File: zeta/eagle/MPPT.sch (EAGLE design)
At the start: 52 parts, among them J1 1.27MM-SWD-CONNECTOR, Q1 ON-NFET, Q2 P-CHANNELFET, U1 TCAN330, U3 LM3671MF-3.3, U6 STM32F042K6, X1 8MHZ-2.5x2mm

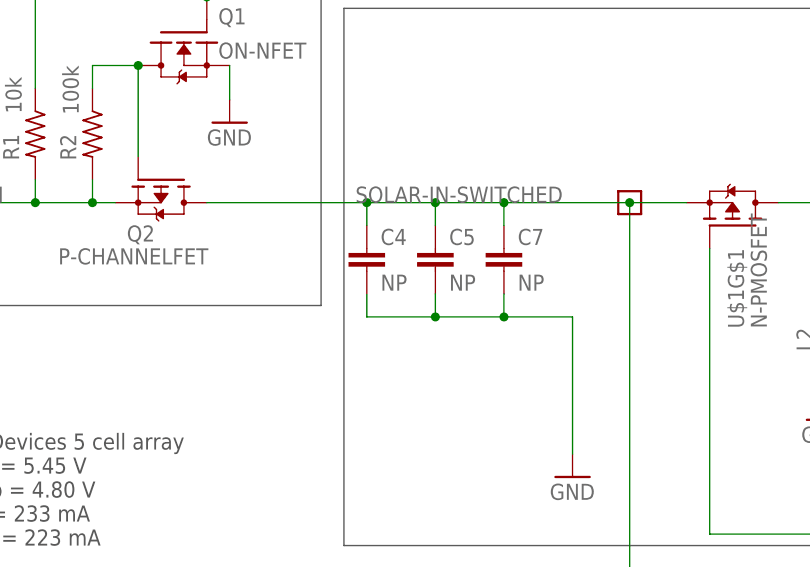
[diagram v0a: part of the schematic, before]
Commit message: Added Breakout Cable Schematic
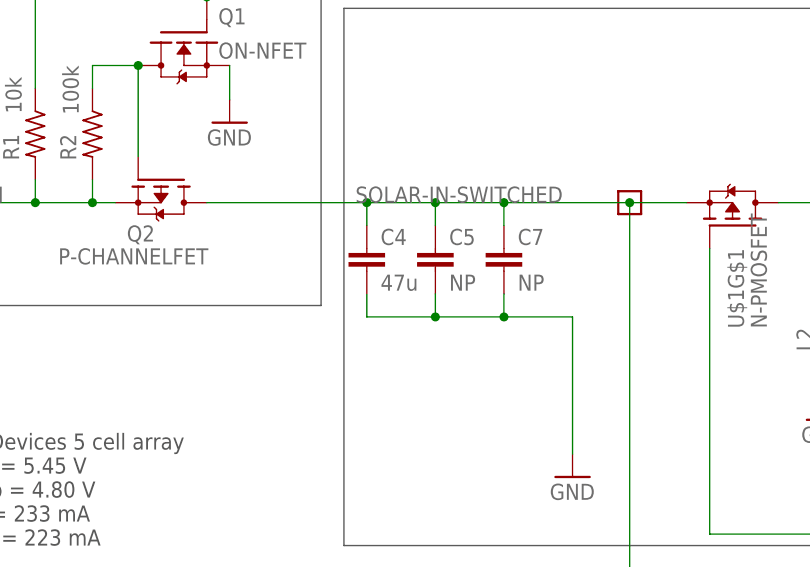
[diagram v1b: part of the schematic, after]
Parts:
- C4: value NP -> 47u
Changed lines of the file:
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@@
 <setting verticaltext="up"/>
 </settings>
-<grid distance="1.27" unitdist="mm" unit="mm" style="lines" multiple="1" display="no" altdistance="0.01" altunitdist="inch" altunit="inch"/>
+<grid distance="0.1" unitdist="inch" unit="inch" style="lines" multiple="1" display="no" altdistance="0.01" altunitdist="inch" altunit="inch"/>
 <layers>
-<layer number="1" name="Top" color="4" fill="1" visible="yes" active="no"/>
-<layer number="2" name="Route2" color="15" fill="1" visible="yes" active="no"/>
-<layer number="3" name="Route3" color="4" fill="3" visible="yes" active="no"/>
-<layer number="4" name="Route4" color="1" fill="4" visible="yes" active="no"/>
-<layer number="5" name="Route5" color="4" fill="4" visible="yes" active="no"/>
-<layer number="6" name="Route6" color="1" fill="8" visible="yes" active="no"/>
-<layer number="7" name="Route7" color="4" fill="8" visible="yes" active="no"/>
-<layer number="8" name="Route8" color="1" fill="2" visible="yes" active="no"/>
-<layer number="9" name="Route9" color="4" fill="2" visible="yes" active="no"/>
-<layer number="10" name="Route10" color="1" fill="7" visible="yes" active="no"/>
-<layer number="11" name="Route11" color="4" fill="7" visible="yes" active="no"/>
-<layer number="12" name="Route12" color="1" fill="5" visible="yes" active="no"/>
-<layer number="13" name="Route13" color="4" fill="5" visible="yes" active="no"/>
-<layer number="14" name="Route14" color="1" fill="6" visible="yes" active="no"/>
-<layer number="15" name="Route15" color="14" fill="1" visible="yes" active="no"/>
-<layer number="16" name="Bottom" color="1" fill="1" visible="yes" active="no"/>
-<layer number="17" name="Pads" color="2" fill="1" visible="yes" active="no"/>
-<layer number="18" name="Vias" color="2" fill="1" visible="yes" active="no"/>
-<layer number="19" name="Unrouted" color="6" fill="1" visible="yes" active="no"/>
-<layer number="20" name="Dimension" color="15" fill="1" visible="yes" active="no"/>
-<layer number="21" name="tPlace" color="7" fill="1" visible="yes" active="no"/>
-<layer number="22" name="bPlace" color="7" fill="1" visible="yes" active="no"/>
-<layer number="23" name="tOrigins" color="15" fill="1" visible="yes" active="no"/>
-<layer number="24" name="bOrigins" color="15" fill="1" visible="yes" active="no"/>
-<layer number="25" name="tNames" color="7" fill="1" visible="yes" active="no"/>
-<layer number="26" name="bNames" color="7" fill="1" visible="yes" active="no"/>
-<layer number="27" name="tValues" color="7" fill="1" visible="yes" active="no"/>
-<layer number="28" name="bValues" color="7" fill="1" visible="yes" active="no"/>
+<layer number="1" name="Top" color="4" fill="1" visible="no" active="no"/>
+<layer number="2" name="Route2" color="15" fill="1" visible="no" active="no"/>
+<layer number="3" name="Route3" color="4" fill="3" visible="no" active="no"/>
+<layer number="4" name="Route4" color="1" fill="4" visible="no" active="no"/>
+<layer number="5" name="Route5" color="4" fill="4" visible="no" active="no"/>
+<layer number="6" name="Route6" color="1" fill="8" visible="no" active="no"/>
+<layer number="7" name="Route7" color="4" fill="8" visible="no" active="no"/>
+<layer number="8" name="Route8" color="1" fill="2" visible="no" active="no"/>
+<layer number="9" name="Route9" color="4" fill="2" visible="no" active="no"/>
+<layer number="10" name="Route10" color="1" fill="7" visible="no" active="no"/>
+<layer number="11" name="Route11" color="4" fill="7" visible="no" active="no"/>
+<layer number="12" name="Route12" color="1" fill="5" visible="no" active="no"/>
+<layer number="13" name="Route13" color="4" fill="5" visible="no" active="no"/>
+<layer number="14" name="Route14" color="1" fill="6" visible="no" active="no"/>
+<layer number="15" name="Route15" color="14" fill="1" visible="no" active="no"/>
+<layer number="16" name="Bottom" color="1" fill="1" visible="no" active="no"/>
+<layer number="17" name="Pads" color="2" fill="1" visible="no" active="no"/>
+<layer number="18" name="Vias" color="2" fill="1" visible="no" active="no"/>
+<layer number="19" name="Unrouted" color="6" fill="1" visible="no" active="no"/>
+<layer number="20" name="Dimension" color="15" fill="1" visible="no" active="no"/>
+<layer number="21" name="tPlace" color="7" fill="1" visible="no" active="no"/>
+<layer number="22" name="bPlace" color="7" fill="1" visible="no" active="no"/>
+<layer number="23" name="tOrigins" color="15" fill="1" visible="no" active="no"/>
+<layer number="24" name="bOrigins" color="15" fill="1" visible="no" active="no"/>
+<layer number="25" name="tNames" color="7" fill="1" visible="no" active="no"/>
+<layer number="26" name="bNames" color="7" fill="1" visible="no" active="no"/>
+<layer number="27" name="tValues" color="7" fill="1" visible="no" active="no"/>
+<layer number="28" name="bValues" color="7" fill="1" visible="no" active="no"/>
 <layer number="29" name="tStop" color="7" fill="3" visible="no" active="no"/>
 <layer number="30" name="bStop" color="7" fill="6" visible="no" active="no"/>
@@
 <layer number="35" name="tGlue" color="7" fill="4" visible="no" active="no"/>
 <layer number="36" name="bGlue" color="7" fill="5" visible="no" active="no"/>
-<layer number="37" name="tTest" color="7" fill="1" visible="yes" active="no"/>
-<layer number="38" name="bTest" color="7" fill="1" visible="yes" active="no"/>
+<layer number="37" name="tTest" color="7" fill="1" visible="no" active="no"/>
+<layer number="38" name="bTest" color="7" fill="1" visible="no" active="no"/>
 <layer number="39" name="tKeepout" color="4" fill="11" visible="no" active="no"/>
 <layer number="40" name="bKeepout" color="1" fill="11" visible="no" active="no"/>
@@
 <layer number="44" name="Drills" color="7" fill="1" visible="no" active="no"/>
 <layer number="45" name="Holes" color="7" fill="1" visible="no" active="no"/>
-<layer number="46" name="Milling" color="3" fill="1" visible="yes" active="no"/>
-<layer number="47" name="Measures" color="7" fill="1" visible="yes" active="no"/>
-<layer number="48" name="Document" color="7" fill="1" visible="yes" active="no"/>
-<layer number="49" name="Reference" color="7" fill="1" visible="yes" active="no"/>
-<layer number="50" name="dxf" color="7" fill="1" visible="yes" active="no"/>
-<layer number="51" name="tDocu" color="7" fill="1" visible="yes" active="no"/>
-<layer number="52" name="bDocu" color="7" fill="1" visible="yes" active="no"/>
-<layer number="53" name="tGND_GNDA" color="7" fill="1" visible="yes" active="no"/>
-<layer number="54" name="bGND_GNDA" color="7" fill="1" visible="yes" active="no"/>
-<layer number="56" name="wert" color="7" fill="1" visible="yes" active="no"/>
-<layer number="57" name="tCAD" color="7" fill="1" visible="yes" active="no"/>
-<layer number="58" name="b3D" color="7" fill="1" visible="yes" active="no"/>
-<layer number="59" name="Invisible" color="7" fill="1" visible="yes" active="no"/>
-<layer number="61" name="stand" color="7" fill="1" visible="yes" active="no"/>
+<layer number="46" name="Milling" color="3" fill="1" visible="no" active="no"/>
+<layer number="47" name="Measures" color="7" fill="1" visible="no" active="no"/>
+<layer number="48" name="Document" color="7" fill="1" visible="no" active="no"/>
+<layer number="49" name="Reference" color="7" fill="1" visible="no" active="no"/>
+<layer number="50" name="dxf" color="7" fill="1" visible="no" active="no"/>
+<layer number="51" name="tDocu" color="7" fill="1" visible="no" active="no"/>
+<layer number="52" name="bDocu" color="7" fill="1" visible="no" active="no"/>
+<layer number="53" name="tGND_GNDA" color="7" fill="1" visible="no" active="no"/>
+<layer number="54" name="bGND_GNDA" color="7" fill="1" visible="no" active="no"/>
+<layer number="56" name="wert" color="7" fill="1" visible="no" active="no"/>
+<layer number="57" name="tCAD" color="7" fill="1" visible="no" active="no"/>
+<layer number="58" name="b3D" color="7" fill="1" visible="no" active="no"/>
+<layer number="59" name="Invisible" color="7" fill="1" visible="no" active="no"/>
+<layer number="61" name="stand" color="7" fill="1" visible="no" active="no"/>
 <layer number="90" name="Modules" color="5" fill="1" visible="yes" active="yes"/>
 <layer number="91" name="Nets" color="2" fill="1" visible="yes" active="yes"/>
@@
 <part name="Q2" library="vishay-p-channel-fet" deviceset="P-CHANNELFET" device=""/>
 <part name="Q1" library="on-n-channel-fet" deviceset="ON-N-CHANNEL-FET" device="" value="ON-NFET"/>
-<part name="C4" library="rcl_custom" deviceset="C-EU" device="C0603" value="NP"/>
+<part name="C4" library="rcl_custom" deviceset="C-EU" device="C0603" value="47u"/>
 <part name="C5" library="rcl_custom" deviceset="C-EU" device="C0603" value="NP"/>
 <part name="C7" library="rcl_custom" deviceset="C-EU" device="C0603" value="NP"/>
